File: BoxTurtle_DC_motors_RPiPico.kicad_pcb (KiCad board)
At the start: 4 copper layers, 99.1 x 73.7 mm, 81 parts, among them J1 Power input, J10 DC motor 1, J11 DC motor 2, J12 DC motor 3, J13 DC motor 4, J14 Screw_Terminal_01x02, J15 CAN, J2 Power input, J3 Power output, J4 Power output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

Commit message: Corrected 5V source for DC motors
As it was this board will blow your USB port.
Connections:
- J6 pad 1: +5V -> +5VBUCK
- J6 pad 2: +5V -> +5VBUCK
- J8 pad 1: +5V -> +5VBUCK
- J8 pad 2: +5V -> +5VBUCK
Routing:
- added copper zone on In2.Cu, net +5VBUCK
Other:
- board text added: "BoxTurtle DC motors standalone board Rev 2.3"
- board text removed: "BoxTurtle DC motors standalone board Rev 2.2"
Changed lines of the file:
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@@
 			(layers "*.Cu" "*.Mask")
 			(remove_unused_layers no)
-			(net 3 "+5V")
+			(net 54 "+5VBUCK")
 			(pinfunction "Pin_1")
 			(pintype "passive")
@@
 			(layers "*.Cu" "*.Mask")
 			(remove_unused_layers no)
-			(net 3 "+5V")
+			(net 54 "+5VBUCK")
 			(pinfunction "Pin_2")
 			(pintype "passive")
@@
 			(layers "*.Cu" "*.Mask")
 			(remove_unused_layers no)
-			(net 3 "+5V")
+			(net 54 "+5VBUCK")
 			(pinfunction "Pin_1")
 			(pintype "passive")
@@
 			(layers "*.Cu" "*.Mask")
 			(remove_unused_layers no)
-			(net 3 "+5V")
+			(net 54 "+5VBUCK")
 			(pinfunction "Pin_2")
 			(pintype "passive")
@@
 		(sheetname "Root")
 		(sheetfile "BoxTurtle_DC_motors_RPiPico.kicad_sch")
-		(attr through_hole exclude_from_pos_files exclude_from_bom)
+		(attr through_hole exclude_from_pos_files)
 		(fp_line
 			(start -7.4 2.4)
@@
 	)
 	(footprint "kibuzzard-67A00B69"
-		(locked yes)
 		(layer "F.Cu")
 		(at 133.985 54.356)
@@
 		(layer "Edge.Cuts")
 	)
-	(gr_text "BoxTurtle DC motors\nstandalone board\nRev 2.2"
+	(gr_text "BoxTurtle DC motors\nstandalone board\nRev 2.3"
 		(at 153.924 79.756 0)
 		(layer "B.SilkS")
@@
 			(justify left mirror)
 		)
-		(render_cache "BoxTurtle DC motors\nstandalone board\nRev 2.2" 0
+		(render_cache "BoxTurtle DC motors\nstandalone board\nRev 2.3" 0
 			(polygon
 				(pts
@@
 			(polygon
 				(pts
-					(xy 144.855263 81.986195) (xy 145.73991 81.986195) (xy 145.835188 82.008753) (xy 145.911982 82.075696)
-					(xy 145.941655 82.170842) (xy 145.941655 82.467842) (xy 145.645144 82.467842) (xy 145.645144 82.327646)
-					(xy 145.588968 82.271959) (xy 145.006693 82.271959) (xy 144.950517 82.327646) (xy 144.950517 82.767284)
-					(xy 145.006693 82.823459) (xy 145.73991 82.823459) (xy 145.835188 82.846017) (xy 145.911982 82.91296)
-					(xy 145.941655 83.008107) (xy 145.941655 83.946) (xy 144.653518 83.946) (xy 144.653518 83.464841)
-					(xy 144.950517 83.464841) (xy 144.950517 83.660724) (xy 145.645144 83.660724) (xy 145.645144 83.164911)
-					(xy 145.588968 83.109224) (xy 144.855263 83.109224) (xy 144.759985 83.086651) (xy 144.68319 83.019585)
-					(xy 144.653518 82.924087) (xy 144.653518 82.170842) (xy 144.68319 82.075696) (xy 144.759985 82.008753)
+					(xy 144.894341 81.986195) (xy 145.779478 81.986195) (xy 145.882851 82.013241) (xy 145.955996 82.083427)
+					(xy 145.980734 82.170842) (xy 145.980734 82.467842) (xy 145.684223 82.467842) (xy 145.684223 82.327646)
+					(xy 145.628047 82.271959) (xy 145.045772 82.271959) (xy 144.989596 82.327646) (xy 144.989596 82.758979)
+					(xy 145.045772 82.815155) (xy 145.630978 82.815155) (xy 145.630978 83.100431) (xy 145.045772 83.100431)
+					(xy 144.989596 83.156607) (xy 144.989596 83.604548) (xy 145.045772 83.660724) (xy 145.628047 83.660724)
+					(xy 145.684223 83.604548) (xy 145.684223 83.464841) (xy 145.980734 83.464841) (xy 145.980734 83.761352)
+					(xy 145.951081 83.856716) (xy 145.874425 83.92354) (xy 145.779478 83.946) (xy 144.894341 83.946)
+					(xy 144.790968 83.919067) (xy 144.717823 83.848984) (xy 144.693085 83.761352) (xy 144.693085 83.134136)
+					(xy 144.719309 83.038155) (xy 144.798414 82.969825) (xy 144.841096 82.957793) (xy 144.748437 82.912958)
+					(xy 144.697967 82.824928) (xy 144.693085 82.78145) (xy 144.693085 82.170842) (xy 144.722738 82.075696)
+					(xy 144.799394 82.008753)
 				)
 			)
@@
 	)
 	(zone
+		(net 54)
+		(net_name "+5VBUCK")
+		(layer "In2.Cu")
+		(hatch edge 0.5)
+		(priority 2)
+		(connect_pads
+			(clearance 0.5)
+		)
+		(min_thickness 0.25)
+		(filled_areas_thickness no)
+		(fill yes
+			(thermal_gap 0.5)
+			(thermal_bridge_width 0.5)
+		)
+		(polygon
+			(pts
+				(xy 151.13 90.805) (xy 151.13 86.995) (xy 146.05 83.185) (xy 146.05 58.42) (xy 137.795 58.42) (xy 137.795 73.025)
+				(xy 122.555 86.36) (xy 122.555 90.805)
+			)
+		)
+	)
+	(zone
 		(net 3)
 		(net_name "+5V")
 		(layer "In2.Cu")
-		(name "5V_plane")
 		(hatch edge 0.5)
 		(priority 1)
@@
 		(polygon
 			(pts
-				(xy 122.555 53.975) (xy 122.555 90.805) (xy 151.765 90.805) (xy 151.765 53.975)
+				(xy 150.495 53.975) (xy 130.175 53.975) (xy 130.175 62.865) (xy 135.255 62.865) (xy 135.255 57.785)
+				(xy 150.495 57.785)
 			)
 		)

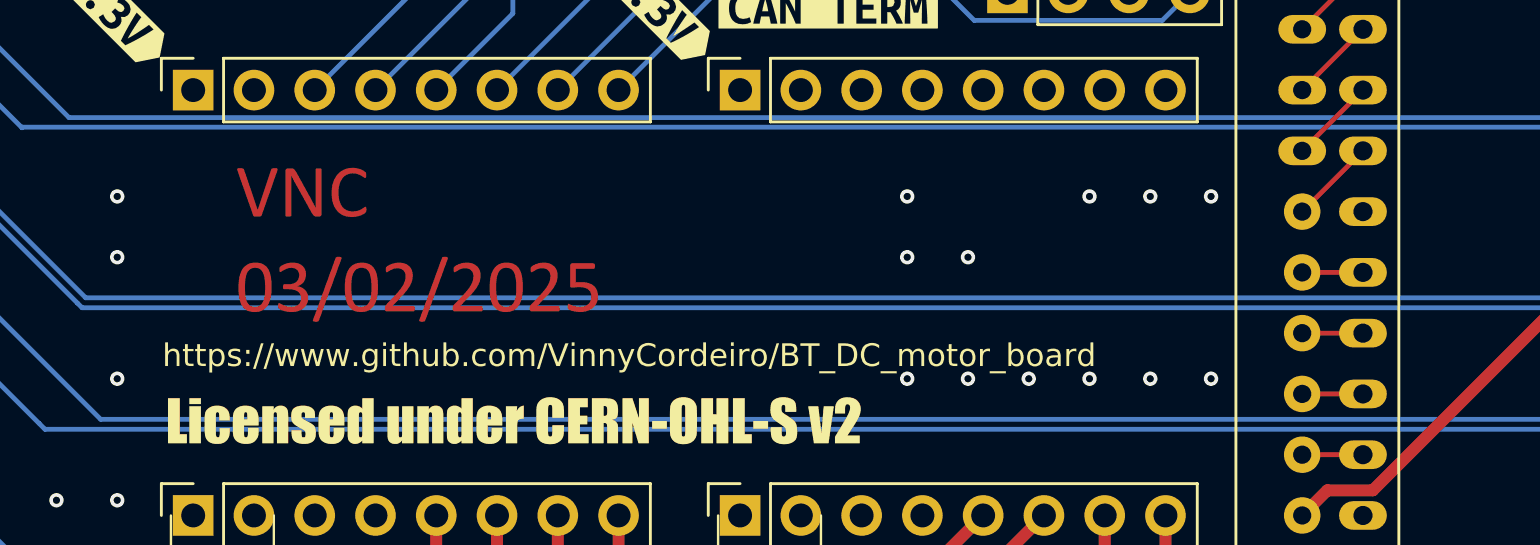
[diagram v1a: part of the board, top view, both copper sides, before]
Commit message: Updated PCB
Modified some more silkscreens, added a fuse 3D model
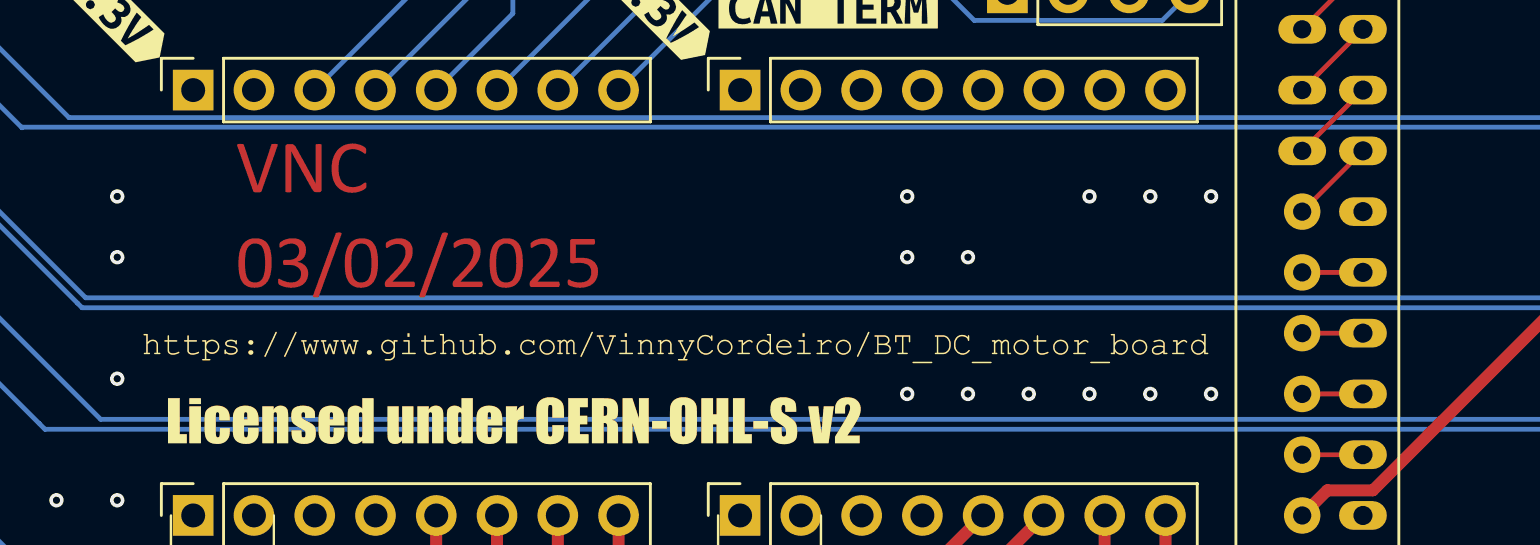
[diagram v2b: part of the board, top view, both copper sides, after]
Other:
- board text removed: "https://www.github.com/VinnyCordeiro/BT_DC_motor_board"

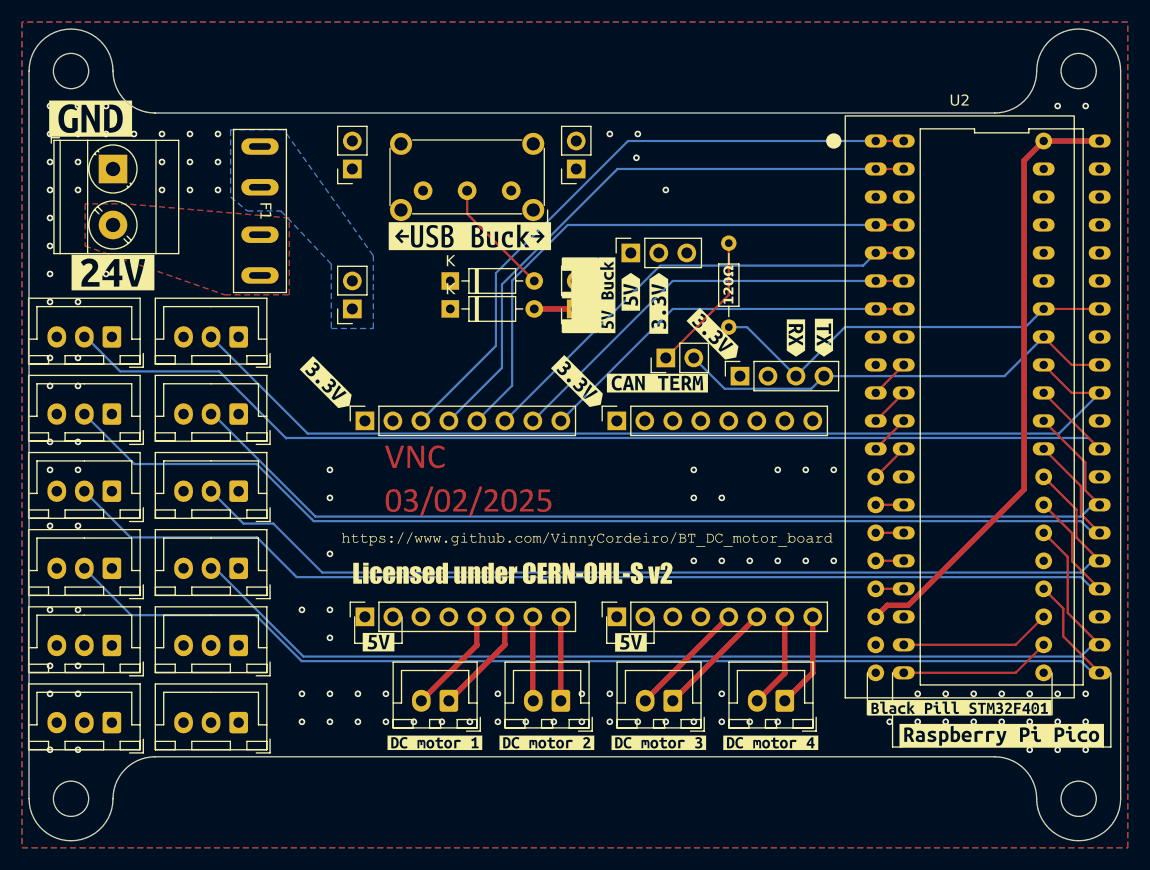
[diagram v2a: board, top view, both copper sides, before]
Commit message: Revision 2.4 - QoL updates
Increased CAN bus resistor footprint; reduced hole diameter on Raspberry Pi Pico's socket pads for snugger fit; changed pin for SW6 on the Black Pill.
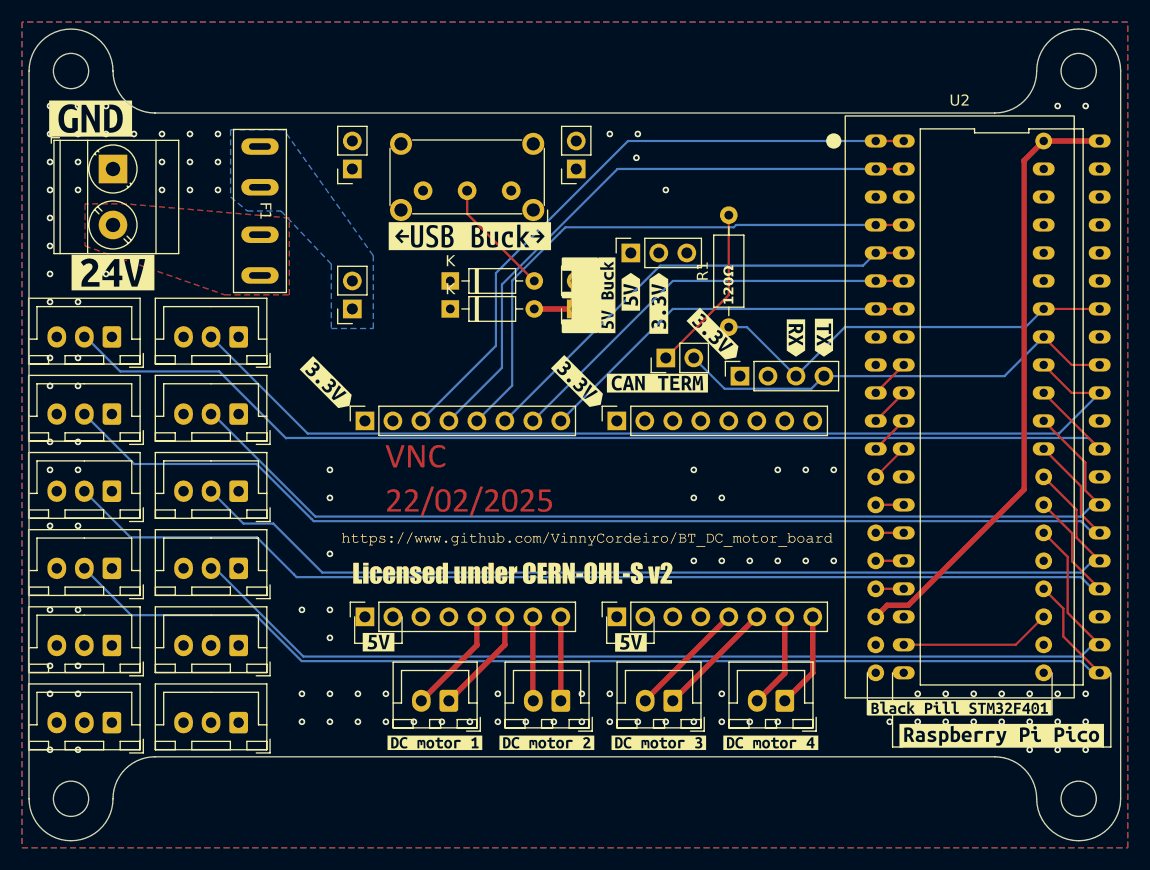
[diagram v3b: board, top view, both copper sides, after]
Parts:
- R1: footprint Resistor_THT:R_Axial_DIN0204_L3.6mm_D1.6mm_P7.62mm_Horizontal -> Resistor_THT:R_Axial_DIN0207_L6.3mm_D2.5mm_P10.16mm_Horizontal
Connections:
- U2 pad 22: SW6 -> unconnected-(U2-PC13-Pad22)
- U2 pad 35: unconnected-(U2-PB1-Pad35) -> SW6
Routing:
- net SW6: track 92.3 -> 120.7 mm
- net Net-(JP1-A): track 12.8 -> 15.3 mm
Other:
- board text added: "BoxTurtle DC motors standalone board Rev 2.4"
- board text removed: "BoxTurtle DC motors standalone board Rev 2.3"

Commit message: Revision 2.5
Corrected the footprint for the 24V to 5V buck converter and the DRV8837 modules.
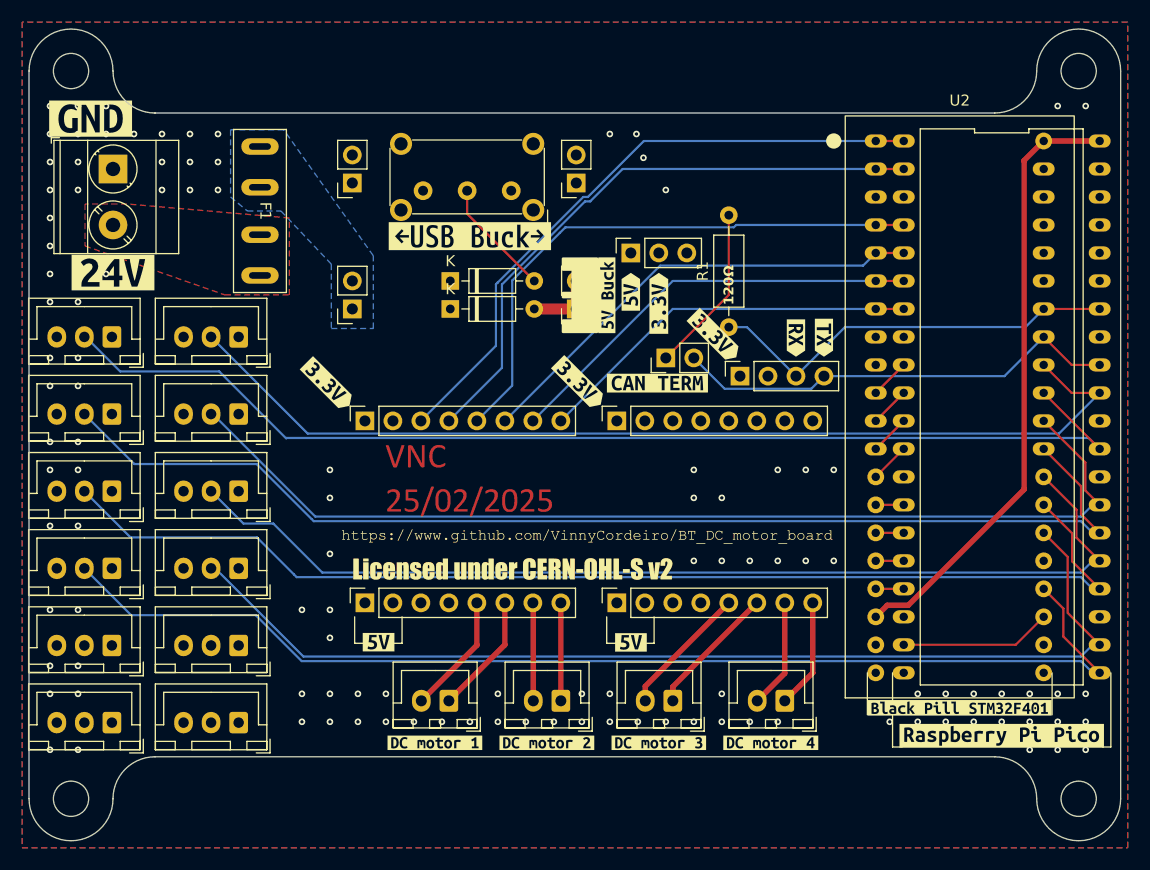
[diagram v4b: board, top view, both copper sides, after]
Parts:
- moved J6 1.27 mm to (124.5, 87.6)
- moved J8 1.27 mm to (147.3, 87.6)
- moved J2 1.27 mm to (123.3, 49.5)
- moved J4 1.27 mm to (143.6, 49.5)
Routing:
- net Net-(J11-Pin_2): track 7.64 -> 8.96 mm
- net Net-(J13-Pin_2): track 8.66 -> 9.93 mm
- net Net-(J13-Pin_1): track 8.67 -> 9.94 mm
- net Net-(J12-Pin_2): track 10.8 -> 12.0 mm
- net Net-(J11-Pin_1): track 7.62 -> 8.89 mm
- net Net-(J10-Pin_2): track 9.71 -> 11.0 mm
- net Net-(J10-Pin_1): track 9.72 -> 11.0 mm
- net Net-(J12-Pin_1): track 10.8 -> 12.0 mm
- net SLP_1: track 58.2 -> 57.6 mm
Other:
- board text added: "BoxTurtle DC motors standalone board Rev 2.5"
- board text removed: "BoxTurtle DC motors standalone board Rev 2.4"
